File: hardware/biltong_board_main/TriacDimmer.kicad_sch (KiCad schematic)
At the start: 20 parts, among them K1 G5Q-1A, Q1 MMBT3904

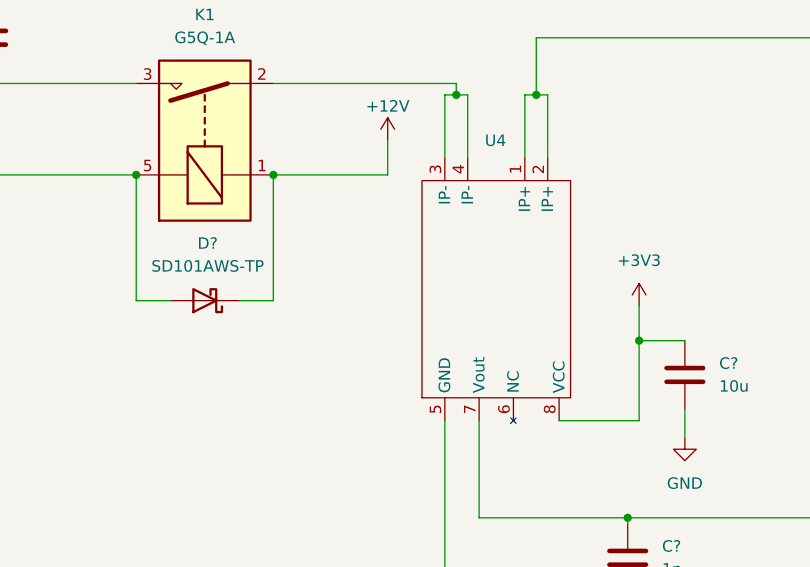
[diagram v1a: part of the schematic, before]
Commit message: generated BOM, swapped 10u cap size, README.md changes
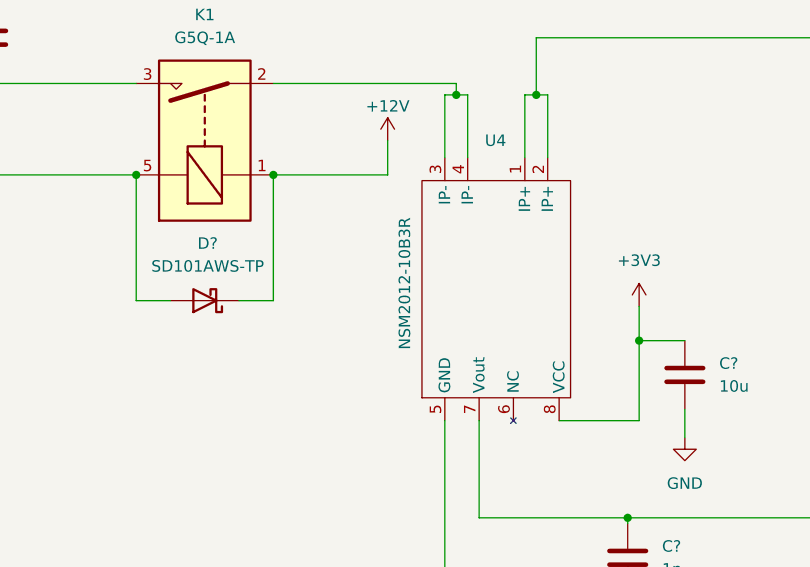
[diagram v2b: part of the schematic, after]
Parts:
- U4: value ~ -> NSM2012-10B3R
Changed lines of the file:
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@@
       (effects (font (size 1.27 1.27)) (justify right))
     )
-    (property "Value" "~" (at 198.12 89.535 0)
+    (property "Value" "NSM2012-10B3R" (at 196.215 76.835 0)
       (effects (font (size 1.27 1.27)))
     )
@@
       (effects (font (size 1.27 1.27)) hide)
     )
-    (property "Datasheet" "~" (at 227.33 86.995 0)
+    (property "Datasheet" "https://www.digikey.ca/en/products/detail/samsung-electro-mechanics/CL10A106MQ8NNNC/3886777" (at 227.33 86.995 0)
       (effects (font (size 1.27 1.27)) hide)
     )
@@
       (effects (font (size 1.27 1.27)) hide)
     )
-    (property "Datasheet" "~" (at 220.98 107.315 0)
-      (effects (font (size 1.27 1.27)) hide)
-    )
+    (property "Datasheet" "https://www.digikey.ca/en/products/detail/kemet/C0603C102K5RACTU/411081" (at 220.98 107.315 0)
+      (effects (font (size 1.27 1.27)) hide)
+    )

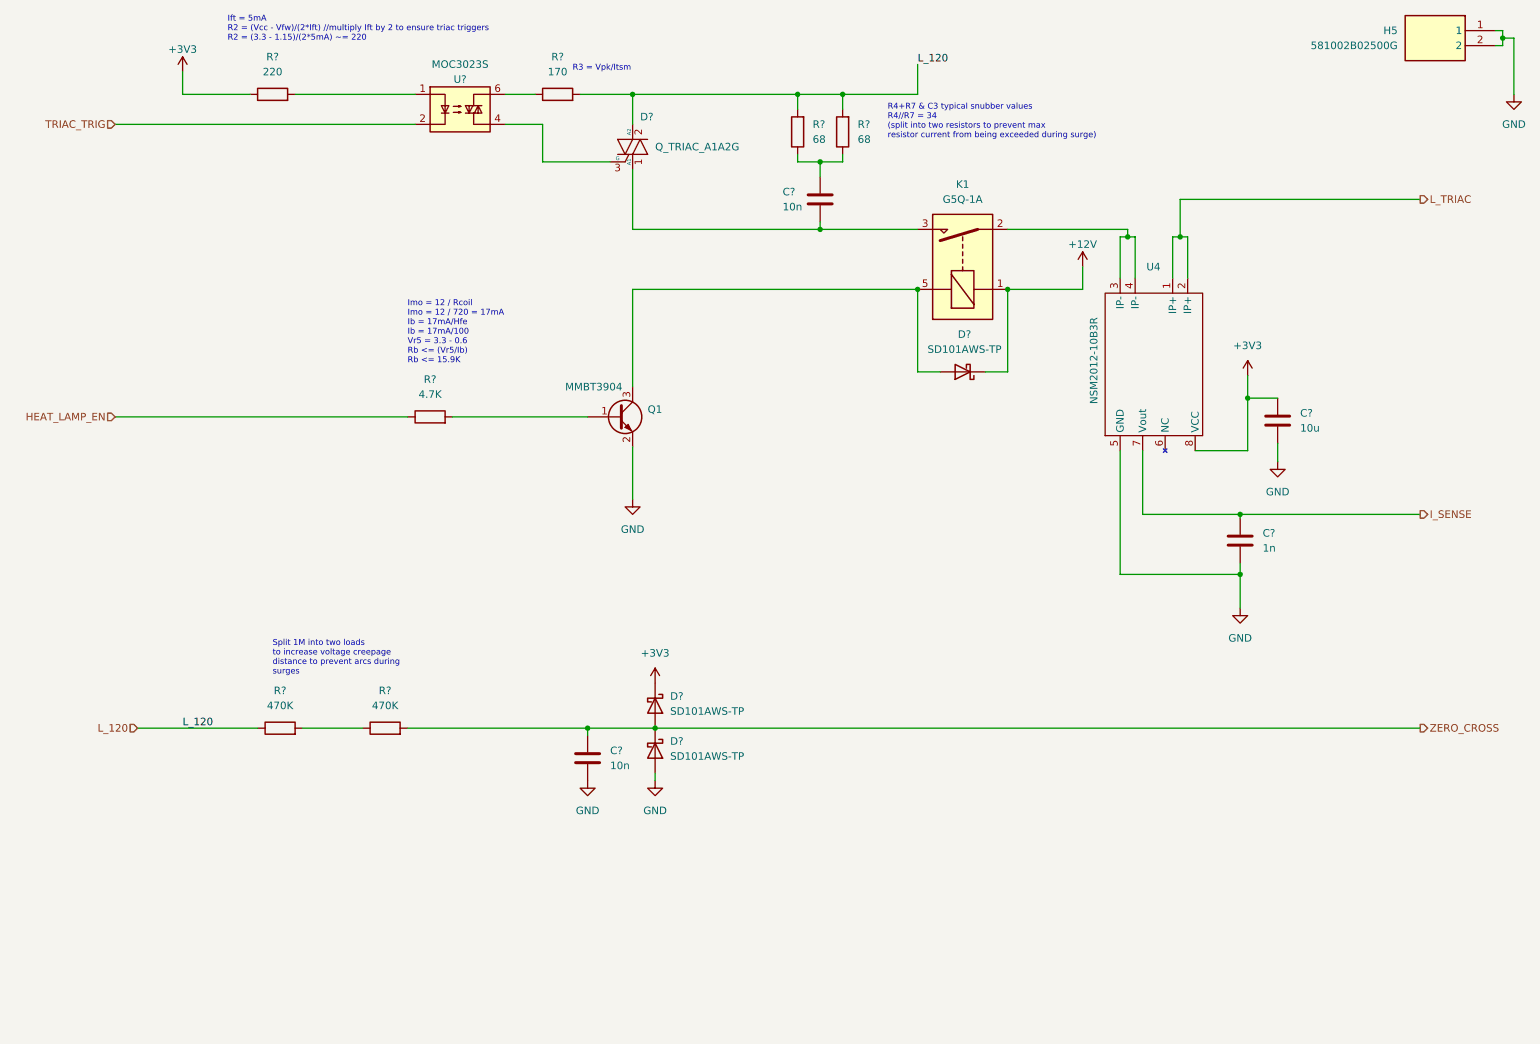
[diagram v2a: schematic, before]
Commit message: Fixed HS1 ground issue, missing schematic values, README.md update
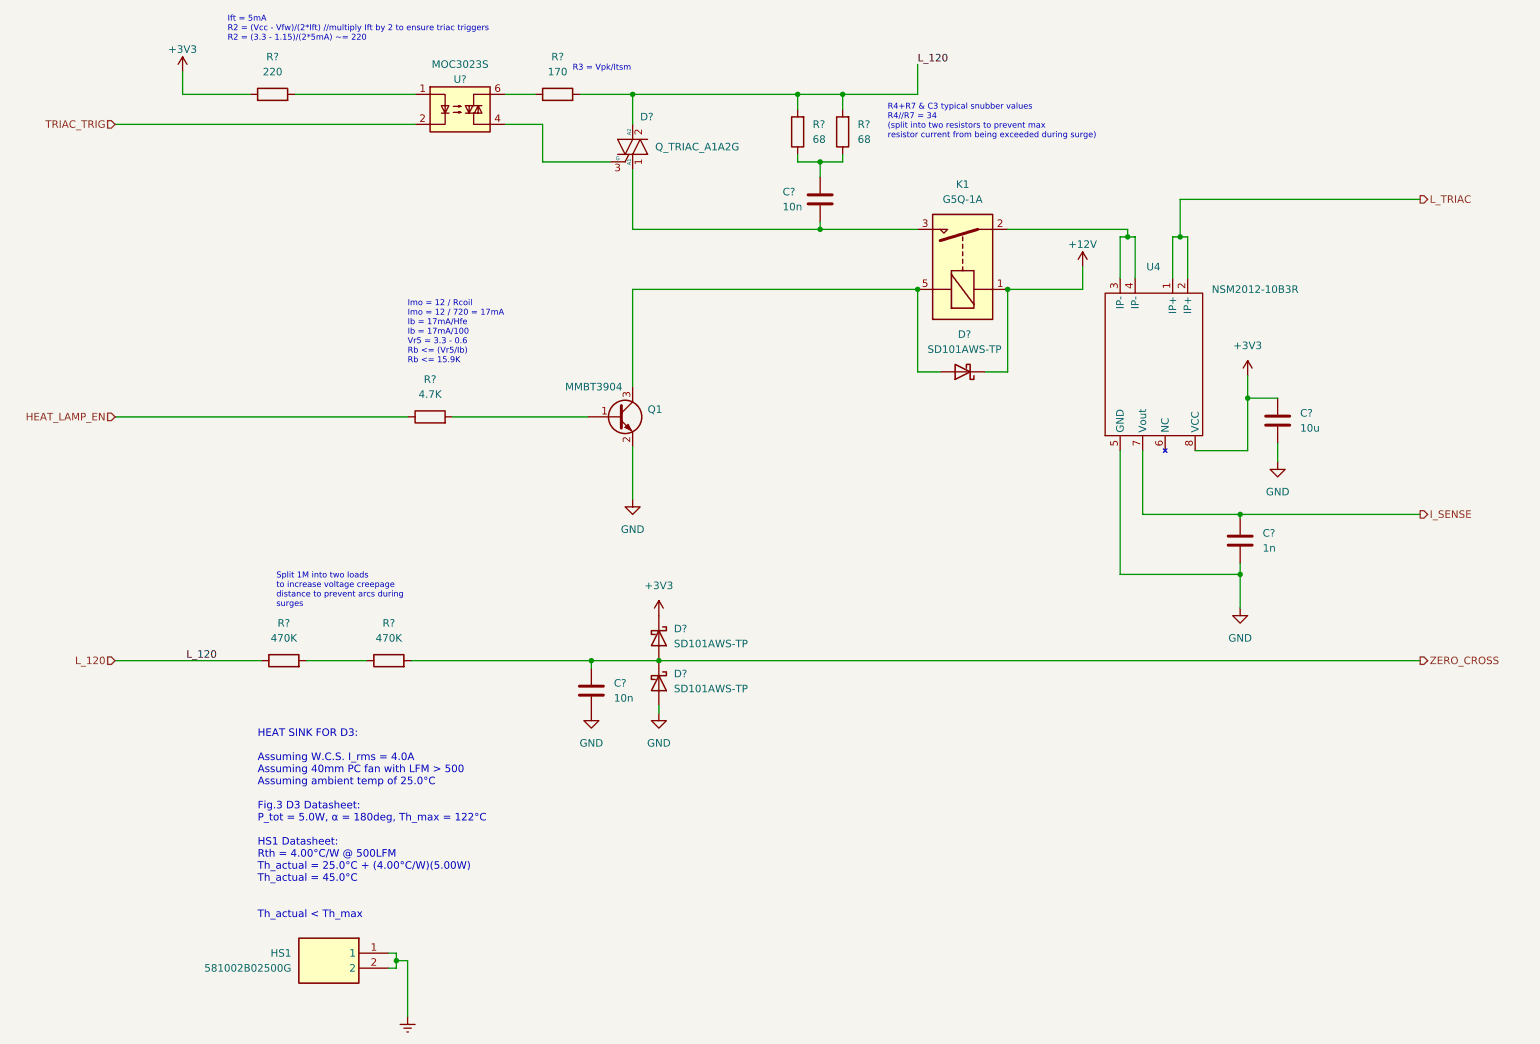
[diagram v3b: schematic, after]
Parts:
- D?: footprint Package_TO_SOT_THT:TO-220-3_Vertical -> BiltongBoardLib:TO-220-3_Vertical_long_pads
- renumbered H5 to HS1
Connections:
- net GND: no longer HS1.1, HS1.2
- new net Earth: HS1.1, HS1.2
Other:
- note added: "HEAT SINK FOR D3: Assuming W.C.S. I_rms = 4.0A Assuming 40mm PC fan with LFM > 500 Assuming ambient temp of 25.0°C Fig.3 D3 Datasheet: P_tot = 5.0W, α = 180deg, Th_max = 122°C HS1 Datasheet: Rth = 4.00°C/W @ 500LFM Th_actual = 25.0°C + (4.00°C/W)(5.00W) Th_actual = 45.0°C Th_actual < Th_max"
- moved on the sheet: C?, D?, HS1, R?

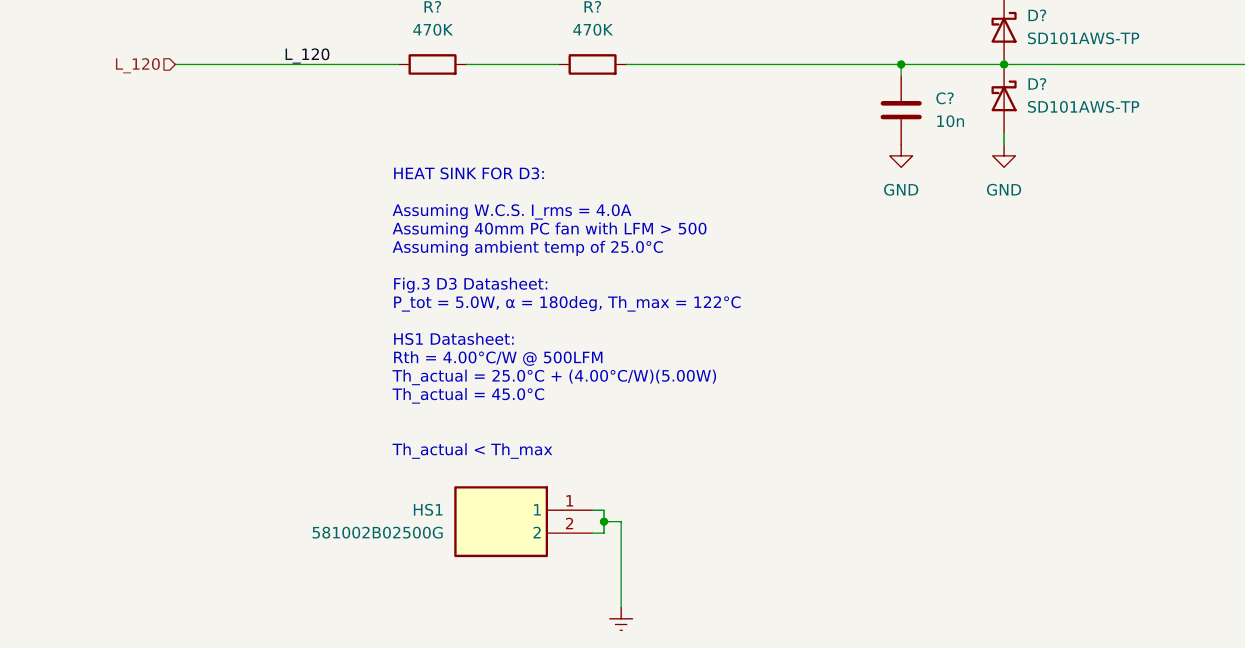
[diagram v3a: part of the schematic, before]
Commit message: swapped zero cross pin for EXTI_2 line, HS1 recalculation
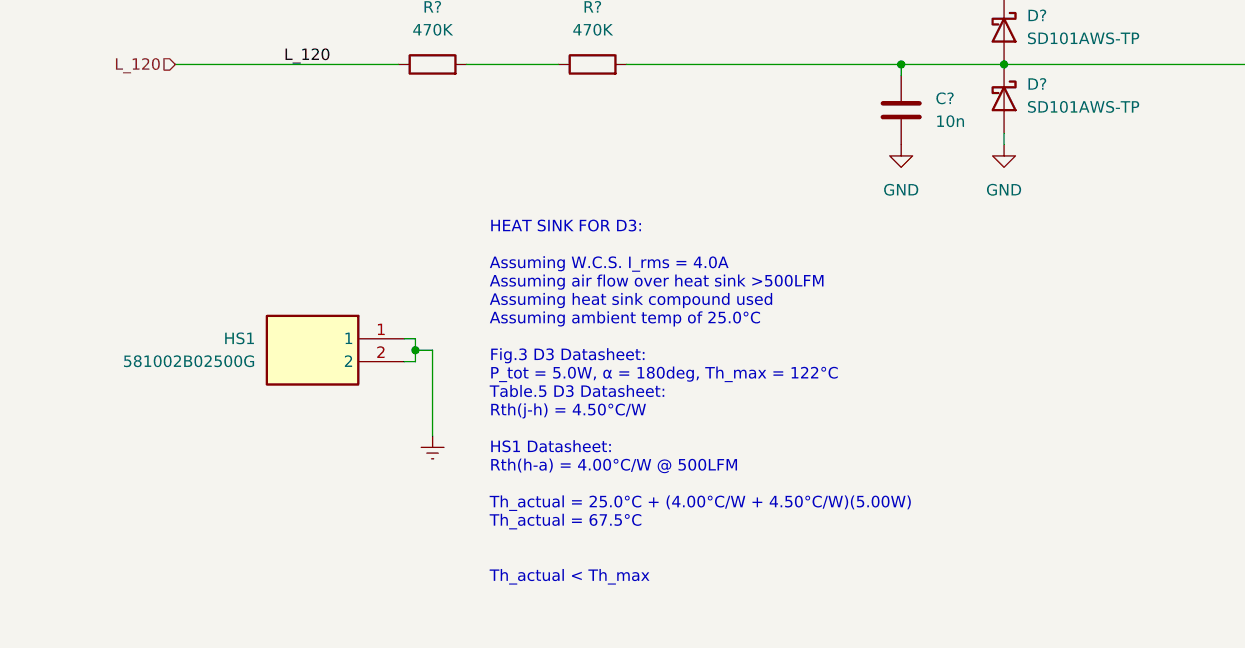
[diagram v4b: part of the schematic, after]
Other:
- note added: "HEAT SINK FOR D3: Assuming W.C.S. I_rms = 4.0A Assuming air flow over heat sink >500LFM Assuming heat sink compound used Assuming ambient temp of 25.0°C Fig.3 D3 Datasheet: P_tot = 5.0W, α = 180deg, Th_max = 122°C Table.5 D3 Datasheet: Rth(j-h) = 4.50°C/W HS1 Datasheet: Rth(h-a) = 4.00°C/W @ 500LFM Th_actual = 25.0°C + (4.00°C/W + 4.50°C/W)(5.00W) Th_actual = 67.5°C Th_actual < Th_max"
- note removed: "HEAT SINK FOR D3: Assuming W.C.S. I_rms = 4.0A Assuming 40mm PC fan with LFM > 500 Assuming ambient temp of 25.0°C Fig.3 D3 Datasheet: P_tot = 5.0W, α = 180deg, Th_max = 122°C HS1 Datasheet: Rth = 4.00°C/W @ 500LFM Th_actual = 25.0°C + (4.00°C/W)(5.00W) Th_actual = 45.0°C Th_actual < Th_max"
- moved on the sheet: HS1
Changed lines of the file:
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@@
   (junction (at 210.82 55.88) (diameter 0) (color 0 0 0 0)
   )
-  (junction (at 78.105 178.435) (diameter 0) (color 0 0 0 0)
+  (junction (at 57.15 159.385) (diameter 0) (color 0 0 0 0)
   )
   (junction (at 220.98 113.03) (diameter 0) (color 0 0 0 0)
@@
     (stroke (width 0) (type default))
   )
-  (wire (pts (xy 76.835 177.165) (xy 78.105 177.165))
+  (wire (pts (xy 55.88 158.115) (xy 57.15 158.115))
     (stroke (width 0) (type default))
   )
@@
     (stroke (width 0) (type default))
   )
-  (wire (pts (xy 80.01 178.435) (xy 80.01 187.96))
-    (stroke (width 0) (type default))
-  )
-  (wire (pts (xy 78.105 177.165) (xy 78.105 178.435))
+  (wire (pts (xy 59.055 159.385) (xy 59.055 168.91))
+    (stroke (width 0) (type default))
+  )
+  (wire (pts (xy 57.15 158.115) (xy 57.15 159.385))
     (stroke (width 0) (type default))
   )
@@
     (stroke (width 0) (type default))
   )
-  (wire (pts (xy 78.105 179.705) (xy 76.835 179.705))
-    (stroke (width 0) (type default))
-  )
-  (wire (pts (xy 78.105 178.435) (xy 80.01 178.435))
+  (wire (pts (xy 57.15 160.655) (xy 55.88 160.655))
+    (stroke (width 0) (type default))
+  )
+  (wire (pts (xy 57.15 159.385) (xy 59.055 159.385))
     (stroke (width 0) (type default))
   )
@@
     (stroke (width 0) (type default))
   )
-  (wire (pts (xy 78.105 178.435) (xy 78.105 179.705))
+  (wire (pts (xy 57.15 159.385) (xy 57.15 160.655))
     (stroke (width 0) (type default))
   )
@@
     (effects (font (size 1 1)) (justify left bottom))
   )
-  (text "HEAT SINK FOR D3:\n\nAssuming W.C.S. I_rms = 4.0A\nAssuming 40mm PC fan with LFM > 500\nAssuming ambient temp of 25.0°C\n\nFig.3 D3 Datasheet:\nP_tot = 5.0W, α = 180deg, Th_max = 122°C\n\nHS1 Datasheet:\nRth = 4.00°C/W @ 500LFM \nTh_actual = 25.0°C + (4.00°C/W)(5.00W)\nTh_actual = 45.0°C\n\n\nTh_actual < Th_max"
-    (at 54.61 171.45 0)
+  (text "HEAT SINK FOR D3:\n\nAssuming W.C.S. I_rms = 4.0A\nAssuming air flow over heat sink >500LFM\nAssuming heat sink compound used\nAssuming ambient temp of 25.0°C\n\nFig.3 D3 Datasheet:\nP_tot = 5.0W, α = 180deg, Th_max = 122°C \nTable.5 D3 Datasheet:\nRth(j-h) = 4.50°C/W\n\nHS1 Datasheet:\nRth(h-a) = 4.00°C/W @ 500LFM \n\nTh_actual = 25.0°C + (4.00°C/W + 4.50°C/W)(5.00W)\nTh_actual = 67.5°C\n\n\nTh_actual < Th_max"
+    (at 65.405 185.42 0)
     (effects (font (size 1.27 1.27)) (justify left bottom))
   )
@@
     )
   )
-  (symbol (lib_id "power:Earth") (at 80.01 187.96 0) (unit 1)
-    (in_bom yes) (on_board yes) (dnp no) (fields_autoplaced)
-    (property "Reference" "#PWR013" (at 80.01 194.31 0)
-      (effects (font (size 1.27 1.27)) hide)
-    )
-    (property "Value" "Earth" (at 80.01 191.77 0)
-      (effects (font (size 1.27 1.27)) hide)
-    )
-    (property "Footprint" "" (at 80.01 187.96 0)
-      (effects (font (size 1.27 1.27)) hide)
-    )
-    (property "Datasheet" "~" (at 80.01 187.96 0)
+  (symbol (lib_id "power:Earth") (at 59.055 168.91 0) (unit 1)
+    (in_bom yes) (on_board yes) (dnp no) (fields_autoplaced)
+    (property "Reference" "#PWR013" (at 59.055 175.26 0)
+      (effects (font (size 1.27 1.27)) hide)
+    )
+    (property "Value" "Earth" (at 59.055 172.72 0)
+      (effects (font (size 1.27 1.27)) hide)
+    )
+    (property "Footprint" "" (at 59.055 168.91 0)
+      (effects (font (size 1.27 1.27)) hide)
+    )
+    (property "Datasheet" "~" (at 59.055 168.91 0)
       (effects (font (size 1.27 1.27)) hide)
     )
@@
     )
   )
-  (symbol (lib_id "BiltongBoard:581002B02500G") (at 76.835 177.165 0) (mirror y) (unit 1)
-    (in_bom yes) (on_board yes) (dnp no) (fields_autoplaced)
-    (property "Reference" "HS1" (at 60.325 177.165 0)
-      (effects (font (size 1.27 1.27)) (justify left))
-    )
-    (property "Value" "581002B02500G" (at 60.325 179.705 0)
-      (effects (font (size 1.27 1.27)) (justify left))
-    )
-    (property "Footprint" "BiltongBoardLib:HSINK_581002B02500G" (at 60.325 272.085 0)
+  (symbol (lib_id "BiltongBoard:581002B02500G") (at 55.88 158.115 0) (mirror y) (unit 1)
+    (in_bom yes) (on_board yes) (dnp no) (fields_autoplaced)
+    (property "Reference" "HS1" (at 39.37 158.115 0)
+      (effects (font (size 1.27 1.27)) (justify left))
+    )
+    (property "Value" "581002B02500G" (at 39.37 160.655 0)
+      (effects (font (size 1.27 1.27)) (justify left))
+    )
+    (property "Footprint" "BiltongBoardLib:HSINK_581002B02500G" (at 39.37 253.035 0)
       (effects (font (size 1.27 1.27)) (justify left top) hide)
     )
-    (property "Datasheet" "https://www.digikey.ca/en/products/detail/boyd-laconia,-llc/581002B02500G/1216391?utm_adgroup=&utm_source=google&utm_medium=cpc&utm_campaign=PMax%20Product_Medium%20ROAS%20Categories&utm_term=&productid=1216391&utm_content=&utm_id=go_cmp-20291741266_adg-_ad-__dev-c_ext-_prd-1216391_sig-CjwKCAjw9p24BhB_EiwA8ID5BlW_YgMOllmkGtcfHg7A3KpRqyWCpoNpV96IIMJXDKDZRuOMo_1otxoCeIAQAvD_BwE&gad_source=1&gclid=CjwKCAjw9p24BhB_EiwA8ID5BlW_YgMOllmkGtcfHg7A3KpRqyWCpoNpV96IIMJXDKDZRuOMo_1otxoCeIAQAvD_BwE" (at 60.325 372.085 0)
+    (property "Datasheet" "https://www.digikey.ca/en/products/detail/boyd-laconia,-llc/581002B02500G/1216391?utm_adgroup=&utm_source=google&utm_medium=cpc&utm_campaign=PMax%20Product_Medium%20ROAS%20Categories&utm_term=&productid=1216391&utm_content=&utm_id=go_cmp-20291741266_adg-_ad-__dev-c_ext-_prd-1216391_sig-CjwKCAjw9p24BhB_EiwA8ID5BlW_YgMOllmkGtcfHg7A3KpRqyWCpoNpV96IIMJXDKDZRuOMo_1otxoCeIAQAvD_BwE&gad_source=1&gclid=CjwKCAjw9p24BhB_EiwA8ID5BlW_YgMOllmkGtcfHg7A3KpRqyWCpoNpV96IIMJXDKDZRuOMo_1otxoCeIAQAvD_BwE" (at 39.37 353.035 0)
       (effects (font (size 1.27 1.27)) (justify left top) hide)
     )
-    (property "Height" "25.4" (at 60.325 572.085 0)
+    (property "Height" "25.4" (at 39.37 553.035 0)
       (effects (font (size 1.27 1.27)) (justify left top) hide)
     )
-    (property "Mouser Part Number" "532-581002B02500G" (at 60.325 672.085 0)
+    (property "Mouser Part Number" "532-581002B02500G" (at 39.37 653.035 0)
       (effects (font (size 1.27 1.27)) (justify left top) hide)
     )
-    (property "Mouser Price/Stock" "https://www.mouser.co.uk/ProductDetail/Aavid/581002B02500G?qs=i82%252BPC3tdLOGMQaV7dyniA%3D%3D" (at 60.325 772.085 0)
+    (property "Mouser Price/Stock" "https://www.mouser.co.uk/ProductDetail/Aavid/581002B02500G?qs=i82%252BPC3tdLOGMQaV7dyniA%3D%3D" (at 39.37 753.035 0)
       (effects (font (size 1.27 1.27)) (justify left top) hide)
     )
-    (property "Manufacturer_Name" "Aavid Thermalloy" (at 60.325 872.085 0)
+    (property "Manufacturer_Name" "Aavid Thermalloy" (at 39.37 853.035 0)
       (effects (font (size 1.27 1.27)) (justify left top) hide)
     )
-    (property "Manufacturer_Part_Number" "581002B02500G" (at 60.325 972.085 0)
+    (property "Manufacturer_Part_Number" "581002B02500G" (at 39.37 953.035 0)
       (effects (font (size 1.27 1.27)) (justify left top) hide)
     )
